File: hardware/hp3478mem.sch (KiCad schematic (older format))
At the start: 8 parts, among them J1 uPD5101LC, J2 PROG_HDR, U1 ATtiny406

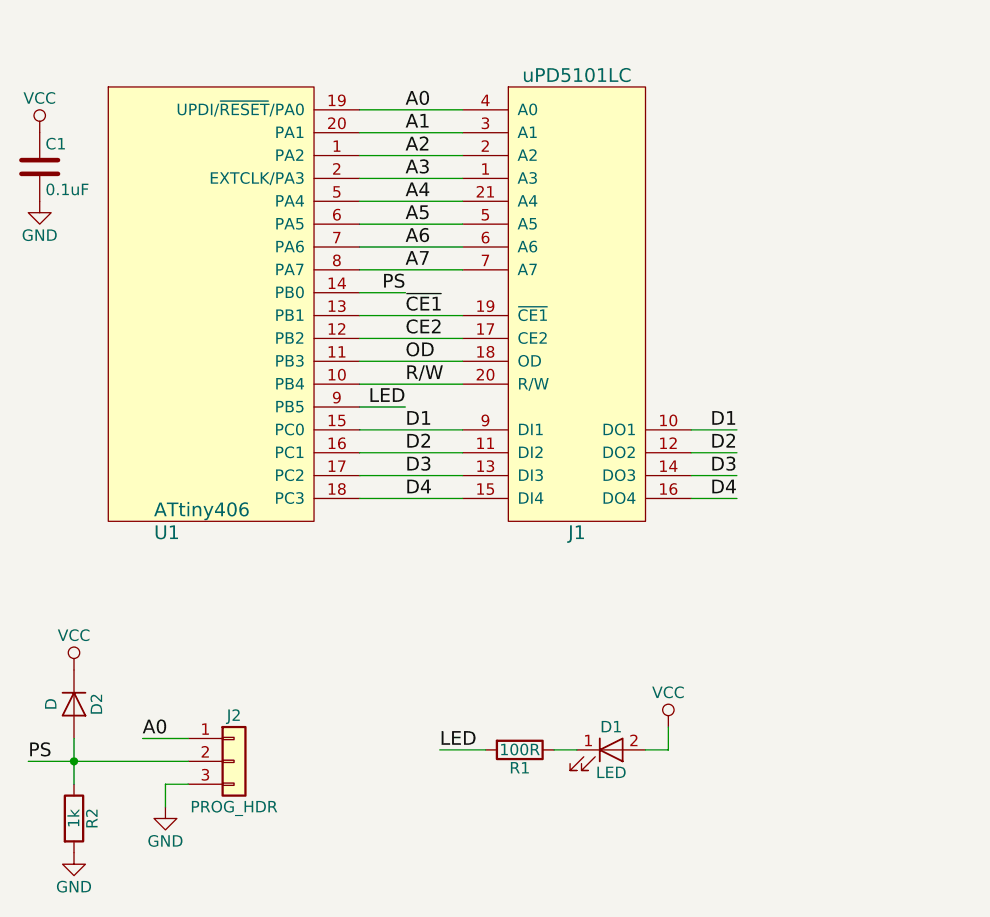
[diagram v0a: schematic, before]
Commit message: Update pad sizes based on issues with prototypes.
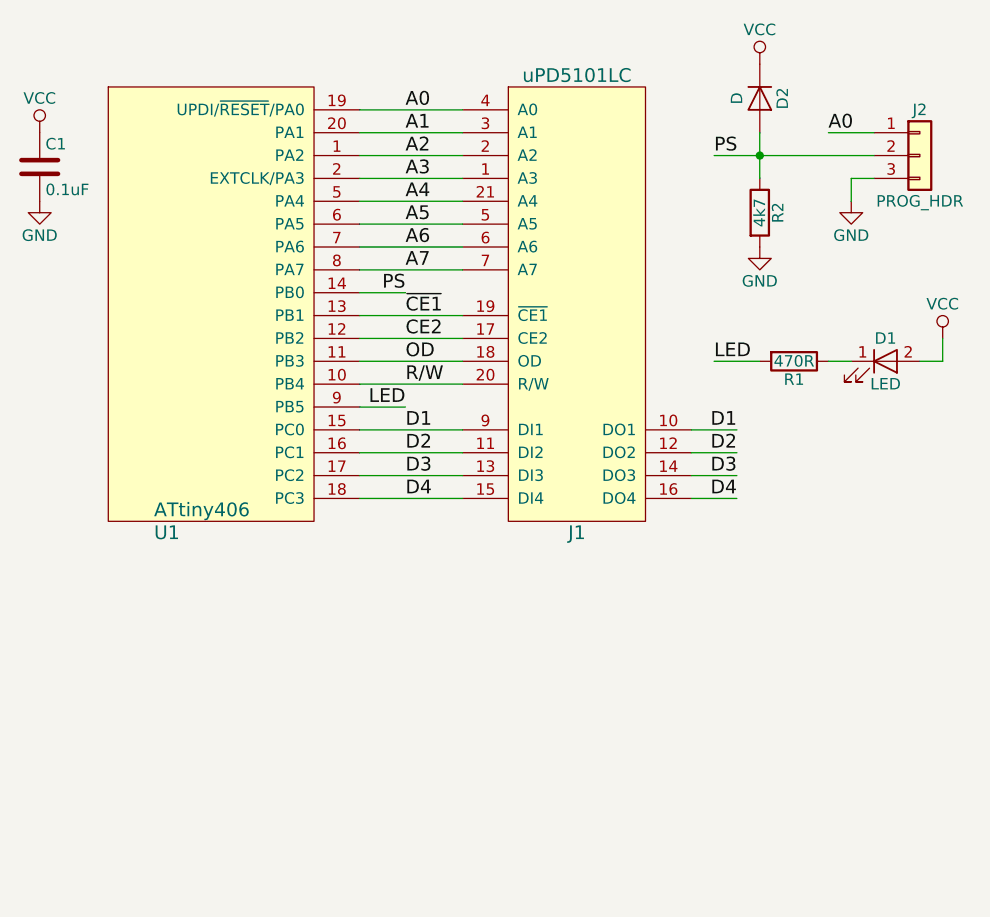
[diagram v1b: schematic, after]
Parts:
- C1: footprint Capacitors_SMD:C_0805_HandSoldering -> Capacitors_SMD:C_0805
- D2: footprint Diodes_SMD:D_0805 -> Diodes_SMD:D_MiniMELF
- R1: value 100R -> 470R; footprint Resistors_SMD:R_0805_HandSoldering -> Resistors_SMD:R_0805
- R2: value 1k -> 4k7; footprint Resistors_SMD:R_0805_HandSoldering -> Resistors_SMD:R_0805
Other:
- moved on the sheet: D1, D2, J2, R1, R2
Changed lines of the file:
@@
 LIBS:valves
 LIBS:custom
+LIBS:hp3478mem-cache
 EELAYER 25 0
 EELAYER END
@@
 F 0 "C1" H 1525 1750 50  0000 L CNN
 F 1 "0.1uF" H 1525 1550 50  0000 L CNN
-F 2 "Capacitors_SMD:C_0805_HandSoldering" H 1538 1500 50  0001 C CNN
+F 2 "Capacitors_SMD:C_0805" H 1538 1500 50  0001 C CNN
 F 3 "" H 1500 1650 50  0001 C CNN
 	1    1500 1650
@@
 L LED D1
 U 1 1 5B2BB0DB
-P 4000 4200
-F 0 "D1" H 4000 4300 50  0000 C CNN
-F 1 "LED" H 4000 4100 50  0000 C CNN
-F 2 "LEDs:LED_0805" H 4000 4200 50  0001 C CNN
-F 3 "" H 4000 4200 50  0001 C CNN
-	1    4000 4200
-	1    0    0    -1
-$EndComp
-Wire Wire Line
-	4150 4200 4250 4200
-Wire Wire Line
-	4250 4200 4250 4100
+P 5200 2500
+F 0 "D1" H 5200 2600 50  0000 C CNN
+F 1 "LED" H 5200 2400 50  0000 C CNN
+F 2 "LEDs:LED_0805" H 5200 2500 50  0001 C CNN
+F 3 "" H 5200 2500 50  0001 C CNN
+	1    5200 2500
+	1    0    0    -1
+$EndComp
+Wire Wire Line
+	5350 2500 5450 2500
+Wire Wire Line
+	5450 2500 5450 2400
 $Comp
 L VCC #PWR03
 U 1 1 5B2BB186
-P 4250 4100
-F 0 "#PWR03" H 4250 3950 50  0001 C CNN
-F 1 "VCC" H 4250 4250 50  0000 C CNN
-F 2 "" H 4250 4100 50  0001 C CNN
-F 3 "" H 4250 4100 50  0001 C CNN
-	1    4250 4100
+P 5450 2400
+F 0 "#PWR03" H 5450 2250 50  0001 C CNN
+F 1 "VCC" H 5450 2550 50  0000 C CNN
+F 2 "" H 5450 2400 50  0001 C CNN
+F 3 "" H 5450 2400 50  0001 C CNN
+	1    5450 2400
 	1    0    0    -1
 $EndComp
@@
 L R R1
 U 1 1 5B2BB1AF
-P 3600 4200
-F 0 "R1" V 3680 4200 50  0000 C CNN
-F 1 "100R" V 3600 4200 50  0000 C CNN
-F 2 "Resistors_SMD:R_0805_HandSoldering" V 3530 4200 50  0001 C CNN
-F 3 "" H 3600 4200 50  0001 C CNN
-	1    3600 4200
+P 4800 2500
+F 0 "R1" V 4880 2500 50  0000 C CNN
+F 1 "470R" V 4800 2500 50  0000 C CNN
+F 2 "Resistors_SMD:R_0805" V 4730 2500 50  0001 C CNN
+F 3 "" H 4800 2500 50  0001 C CNN
+	1    4800 2500
 	0    1    1    0
 $EndComp
 Wire Wire Line
-	3850 4200 3750 4200
-Wire Wire Line
-	3450 4200 3250 4200
-Text Label 3250 4200 0    60   ~ 0
+	5050 2500 4950 2500
+Wire Wire Line
+	4650 2500 4450 2500
+Text Label 4450 2500 0    60   ~ 0
 LED
 Wire Wire Line
-	2150 4350 2050 4350
-Wire Wire Line
-	2050 4350 2050 4450
+	5150 1700 5050 1700
+Wire Wire Line
+	5050 1700 5050 1800
 $Comp
 L GND #PWR04
 U 1 1 5B2BB5B0
-P 2050 4450
-F 0 "#PWR04" H 2050 4200 50  0001 C CNN
-F 1 "GND" H 2050 4300 50  0000 C CNN
-F 2 "" H 2050 4450 50  0001 C CNN
-F 3 "" H 2050 4450 50  0001 C CNN
-	1    2050 4450
+P 5050 1800
+F 0 "#PWR04" H 5050 1550 50  0001 C CNN
+F 1 "GND" H 5050 1650 50  0000 C CNN
+F 2 "" H 5050 1800 50  0001 C CNN
+F 3 "" H 5050 1800 50  0001 C CNN
+	1    5050 1800
 	1    0    0    -1
 $EndComp
@@
 L D D2
 U 1 1 5B2BB5D0
-P 1650 4000
-F 0 "D2" H 1650 4100 50  0000 C CNN
-F 1 "D" H 1650 3900 50  0000 C CNN
-F 2 "Diodes_SMD:D_0805" H 1650 4000 50  0001 C CNN
-F 3 "" H 1650 4000 50  0001 C CNN
-	1    1650 4000
+P 4650 1350
+F 0 "D2" H 4650 1450 50  0000 C CNN
+F 1 "D" H 4650 1250 50  0000 C CNN
+F 2 "Diodes_SMD:D_MiniMELF" H 4650 1350 50  0001 C CNN
+F 3 "" H 4650 1350 50  0001 C CNN
+	1    4650 1350
 	0    1    1    0
 $EndComp
 Wire Wire Line
-	1450 4250 2150 4250
+	4450 1600 5150 1600
 $Comp
 L VCC #PWR05
 U 1 1 5B2BB693
-P 1650 3850
-F 0 "#PWR05" H 1650 3700 50  0001 C CNN
-F 1 "VCC" H 1650 4000 50  0000 C CNN
-F 2 "" H 1650 3850 50  0001 C CNN
-F 3 "" H 1650 3850 50  0001 C CNN
-	1    1650 3850
+P 4650 1200
+F 0 "#PWR05" H 4650 1050 50  0001 C CNN
+F 1 "VCC" H 4650 1350 50  0000 C CNN
+F 2 "" H 4650 1200 50  0001 C CNN
+F 3 "" H 4650 1200 50  0001 C CNN
+	1    4650 1200
 	1    0    0    -1
 $EndComp
@@
 L R R2
 U 1 1 5B2BB707
-P 1650 4500
-F 0 "R2" V 1730 4500 50  0000 C CNN
-F 1 "1k" V 1650 4500 50  0000 C CNN
-F 2 "Resistors_SMD:R_0805_HandSoldering" V 1580 4500 50  0001 C CNN
-F 3 "" H 1650 4500 50  0001 C CNN
-	1    1650 4500
-	1    0    0    -1
-$EndComp
-Wire Wire Line
-	1650 4150 1650 4350
-Text Label 1450 4250 0    60   ~ 0
+P 4650 1850
+F 0 "R2" V 4730 1850 50  0000 C CNN
+F 1 "4k7" V 4650 1850 50  0000 C CNN
+F 2 "Resistors_SMD:R_0805" V 4580 1850 50  0001 C CNN
+F 3 "" H 4650 1850 50  0001 C CNN
+	1    4650 1850
+	1    0    0    -1
+$EndComp
+Wire Wire Line
+	4650 1500 4650 1700
+Text Label 4450 1600 0    60   ~ 0
 PS
 $Comp
 L Conn_01x03 J2
 U 1 1 5B2BB875
-P 2350 4250
-F 0 "J2" H 2350 4450 50  0000 C CNN
-F 1 "PROG_HDR" H 2350 4050 50  0000 C CNN
-F 2 "Pin_Headers:Pin_Header_Straight_1x03_Pitch2.54mm" H 2350 4250 50  0001 C CNN
-F 3 "" H 2350 4250 50  0001 C CNN
-	1    2350 4250
-	1    0    0    -1
-$EndComp
-Wire Wire Line
-	2150 4150 1950 4150
-Text Label 1950 4150 0    60   ~ 0
+P 5350 1600
+F 0 "J2" H 5350 1800 50  0000 C CNN
+F 1 "PROG_HDR" H 5350 1400 50  0000 C CNN
+F 2 "Pin_Headers:Pin_Header_Straight_1x03_Pitch2.54mm" H 5350 1600 50  0001 C CNN
+F 3 "" H 5350 1600 50  0001 C CNN
+	1    5350 1600
+	1    0    0    -1
+$EndComp
+Wire Wire Line
+	5150 1500 4950 1500
+Text Label 4950 1500 0    60   ~ 0
 A0
-Connection ~ 1650 4250
+Connection ~ 4650 1600
 $Comp
 L GND #PWR06
 U 1 1 5B2BC0AD
-P 1650 4650
-F 0 "#PWR06" H 1650 4400 50  0001 C CNN
-F 1 "GND" H 1650 4500 50  0000 C CNN
-F 2 "" H 1650 4650 50  0001 C CNN
-F 3 "" H 1650 4650 50  0001 C CNN
-	1    1650 4650
-	1    0    0    -1
-$EndComp
+P 4650 2000
+F 0 "#PWR06" H 4650 1750 50  0001 C CNN
+F 1 "GND" H 4650 1850 50  0000 C CNN
+F 2 "" H 4650 2000 50  0001 C CNN
+F 3 "" H 4650 2000 50  0001 C CNN
+	1    4650 2000
+	1    0    0    -1
+$EndComp
